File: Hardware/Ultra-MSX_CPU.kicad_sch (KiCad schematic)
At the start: 23 parts, among them J11 Conn_02x05_Odd_Even, J15 Battery_2x_SR66_holder, U1 MPU_Z380, U5 BQ4802YPW, Y2 Crystal_AB38T-32.768KHZ

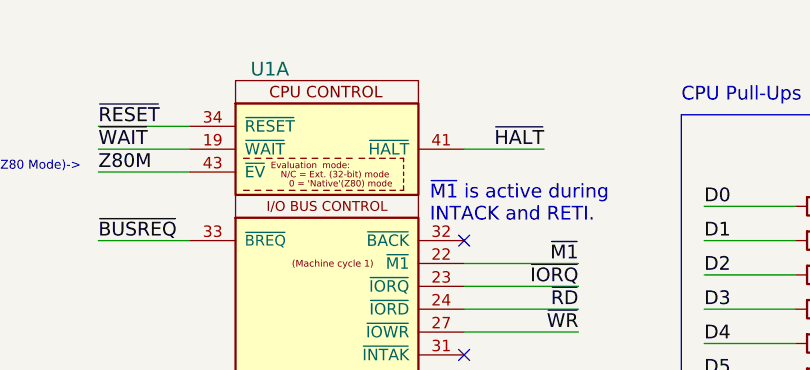
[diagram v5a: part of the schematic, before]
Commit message: Reworked the Printer-port 3D model, and the Scart 3D-model. Generated a 3D model of the main board. Moved peripheral components from separate expansion-headers, to a singular IO-shield board.
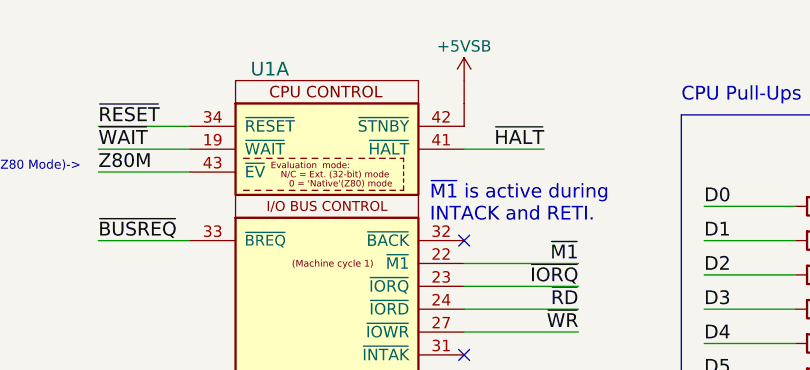
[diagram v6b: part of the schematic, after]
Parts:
- added virt_sym1: Virtual_symbol, LRJ:TestPoint_Bridge_Pitch1.5mm_Pad0.8mm, symbol LRJ-parts:Virtual_symbol
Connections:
- net +5VSB: now also virt_sym1.1
- new net: U1.42 (~{STNBY}), virt_sym1.1
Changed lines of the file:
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@@
     )
   )
-  (symbol (lib_id "Ultra-MSX:MPU_Z380") (at 52.07 54.61 0) (unit 1)
+  (symbol (lib_name "MPU_Z380_2") (lib_id "Ultra-MSX:MPU_Z380") (at 52.07 54.61 0) (unit 1)
     (in_bom yes) (on_board yes)
     (property "Reference" "U1" (id 0) (at 45.72 20.32 0)
@@
     (pin "40")
     (pin "41")
+    (pin "42")
     (pin "43")
     (pin "11")
@@
     (pin "29")
     (pin "30")
-    (pin "42")
     (pin "50")
     (pin "51")
@@
     (pin "40")
     (pin "41")
+    (pin "42")
     (pin "43")
     (pin "11")
@@
     (pin "29")
     (pin "30")
-    (pin "42")
     (pin "50")
     (pin "51")
@@
     (pin "90")
   )
-  (symbol (lib_id "Ultra-MSX:MPU_Z380") (at 135.89 48.26 0) (mirror y) (unit 3)
+  (symbol (lib_name "MPU_Z380_3") (lib_id "Ultra-MSX:MPU_Z380") (at 135.89 48.26 0) (mirror y) (unit 3)
     (in_bom yes) (on_board yes)
     (property "Reference" "U1" (id 0) (at 138.43 24.13 0)
@@
     (pin "40")
     (pin "41")
+    (pin "42")
     (pin "43")
     (pin "11")
@@
     (pin "29")
     (pin "30")
-    (pin "42")
     (pin "50")
     (pin "51")
@@
     (pin "90")
   )
-  (symbol (lib_id "Ultra-MSX:MPU_Z380") (at 226.06 60.96 0) (unit 4)
+  (symbol (lib_name "MPU_Z380_1") (lib_id "Ultra-MSX:MPU_Z380") (at 226.06 60.96 0) (unit 4)
     (in_bom yes) (on_board yes)
     (property "Reference" "U1" (id 0) (at 226.06 19.05 0)
@@
     (pin "40")
     (pin "41")
+    (pin "42")
     (pin "43")
     (pin "11")
@@
     (pin "29")
     (pin "30")
-    (pin "42")
     (pin "50")
     (pin "51")
@@
     (pin "2")
   )
+  (symbol (lib_id "LRJ-parts:+5VSB") (at 67.31 21.59 0) (unit 1)
+    (in_bom no) (on_board yes)
+    (property "Reference" "#PWR034" (id 0) (at 67.31 25.4 0)
+      (effects (font (size 1.27 1.27)) hide)
+    )
+    (property "Value" "+5VSB" (id 1) (at 67.31 17.78 0))
+    (property "Footprint" "" (id 2) (at 67.31 21.59 0)
+      (effects (font (size 1.27 1.27)) hide)
+    )
+    (property "Datasheet" "" (id 3) (at 67.31 21.59 0)
+      (effects (font (size 1.27 1.27)) hide)
+    )
+    (property "Description" "Standby-power, 10 mA max (ATX v.1.x) or  2A max (ATX v.2.2+)" (id 4) (at 67.31 31.75 0)
+      (effects (font (size 1.27 1.27)) hide)
+    )
+    (pin "1")
+  )
+  (symbol (lib_id "LRJ-parts:Virtual_symbol") (at 67.31 24.13 0) (unit 1)
+    (in_bom no) (on_board no) (fields_autoplaced)
+    (property "Reference" "virt_sym1" (id 0) (at 72.39 21.59 0)
+      (effects (font (size 1.27 1.27)) hide)
+    )
+    (property "Value" "Virtual_symbol" (id 1) (at 74.93 24.13 0)
+      (effects (font (size 1.27 1.27)) hide)
+    )
+    (property "Footprint" "LRJ:TestPoint_Bridge_Pitch1.5mm_Pad0.8mm" (id 2) (at 67.945 33.02 0)
+      (effects (font (size 1.27 1.27)) hide)
+    )
+    (property "Datasheet" "" (id 3) (at 69.85 21.59 0)
+      (effects (font (size 1.27 1.27)) hide)
+    )
+    (pin "1")
+    (pin "1")
+  )
   (symbol (lib_id "power:GND") (at 53.34 171.45 90) (unit 1)
